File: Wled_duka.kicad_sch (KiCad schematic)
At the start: 47 parts, among them J1 7775-2, J2 DATA channels, J3 CH1&2, J4 CH3&4, J5 Relay out, J6 DMX512, J7 7775-2, J8 Vin_alt, Q1 DMN3067L-7, U1 ADM3485xR, U2 LMR51420, U3 74AHCT125, U4 ESP32_S3_supermini

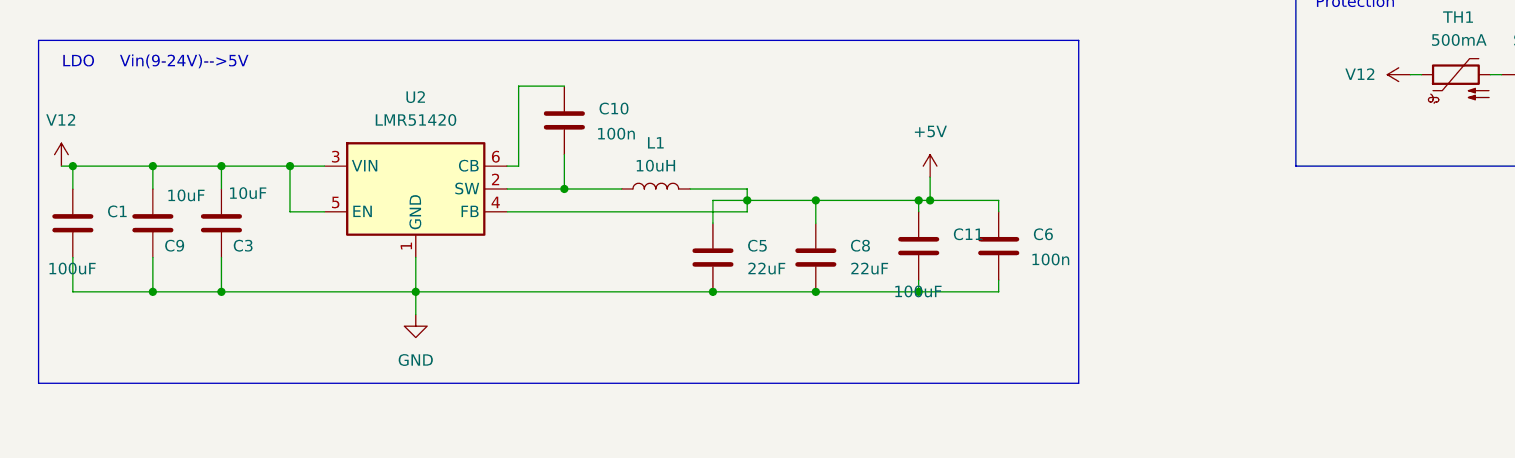
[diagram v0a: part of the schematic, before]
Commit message: Add FB resistors to DC-DC conv.
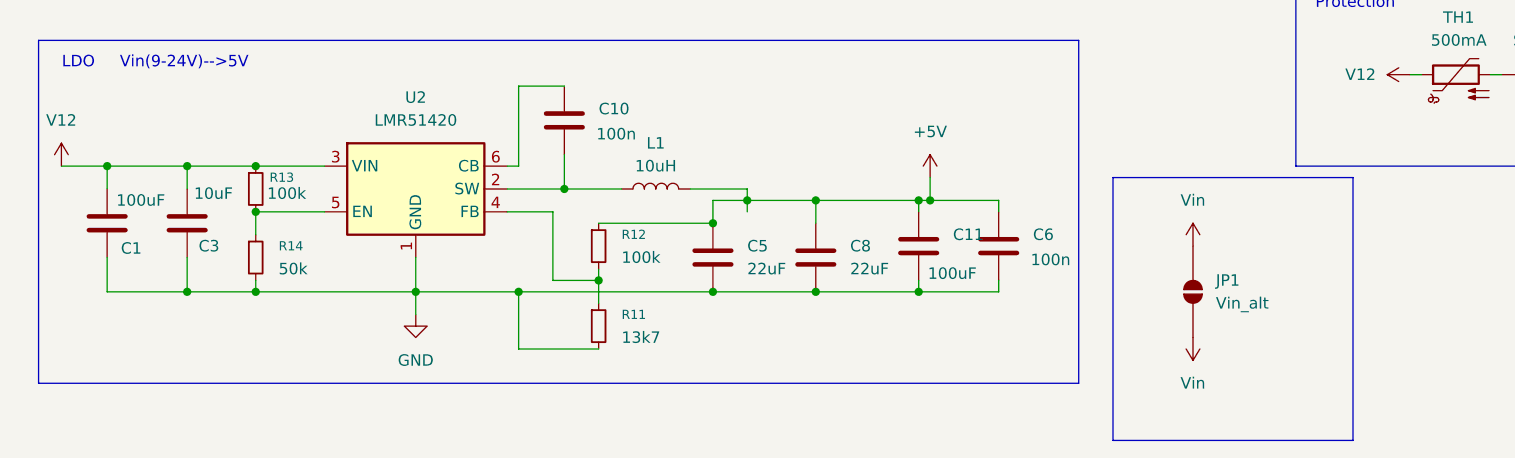
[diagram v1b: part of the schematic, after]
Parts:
- removed C9: 10uF, Capacitor_SMD:C_0805_2012Metric_Pad1.18x1.45mm_HandSolder, symbol Device:C
- added JP1: Vin_alt, Jumper:SolderJumper-2_P1.3mm_Open_RoundedPad1.0x1.5mm, symbol Jumper:SolderJumper_2_Open
- added R11: 13k7, Resistor_SMD:R_0805_2012Metric_Pad1.20x1.40mm_HandSolder, symbol Device:R_Small
- added R12, R13: 100k, Resistor_SMD:R_0805_2012Metric_Pad1.20x1.40mm_HandSolder, symbol Device:R_Small
- added R14: 50k, Resistor_SMD:R_0805_2012Metric_Pad1.20x1.40mm_HandSolder, symbol Device:R_Small
- C10, C4, C6, C7: Mouser Part Number 603-AC402KRX7R9BB104 -> 603-AC0805KKX7R9BB10
- C3: footprint Capacitor_SMD:C_0805_2012Metric_Pad1.18x1.45mm_HandSolder -> Capacitor_SMD:C_1206_3216Metric_Pad1.33x1.80mm_HandSolder; Mouser Part Number 603-AC805KKX7R6BB106 -> 603-CC1206KKX7GBB106
- U4: now left out of the parts list
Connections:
- net +5V: now also R12.1; no longer U2.4 (FB)
- net GND: now also R11.2, R14.2
- net V12: now also R13.1; no longer U2.5 (EN)
- net Vin: now also JP1.1 (A), JP1.2 (B)
- new net: R13.2, R14.1, U2.5 (EN)
- new net: R11.1, R12.2, U2.4 (FB)
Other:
- moved on the sheet: C1, C3

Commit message: CAN transceiver 100nF cap
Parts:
- added C9: 100n, Capacitor_SMD:C_0805_2012Metric_Pad1.18x1.45mm_HandSolder, symbol Device:C
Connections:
- net +3,3V: now also C9.1
- net GND: now also C9.2
